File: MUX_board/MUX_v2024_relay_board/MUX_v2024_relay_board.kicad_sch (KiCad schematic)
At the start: 21 parts, among them J1 A B M N, J2 Relays Pwr, J3 I2C, J4 Screw_Terminal_01x08, J5 A B M N, J6 I2C, U1 24LC02, U2 MCP23017_SP, U3 MCP23017_SP, U4 MCP23017_SP, U5 4052, U6 4052, U7 4052, U8 4052

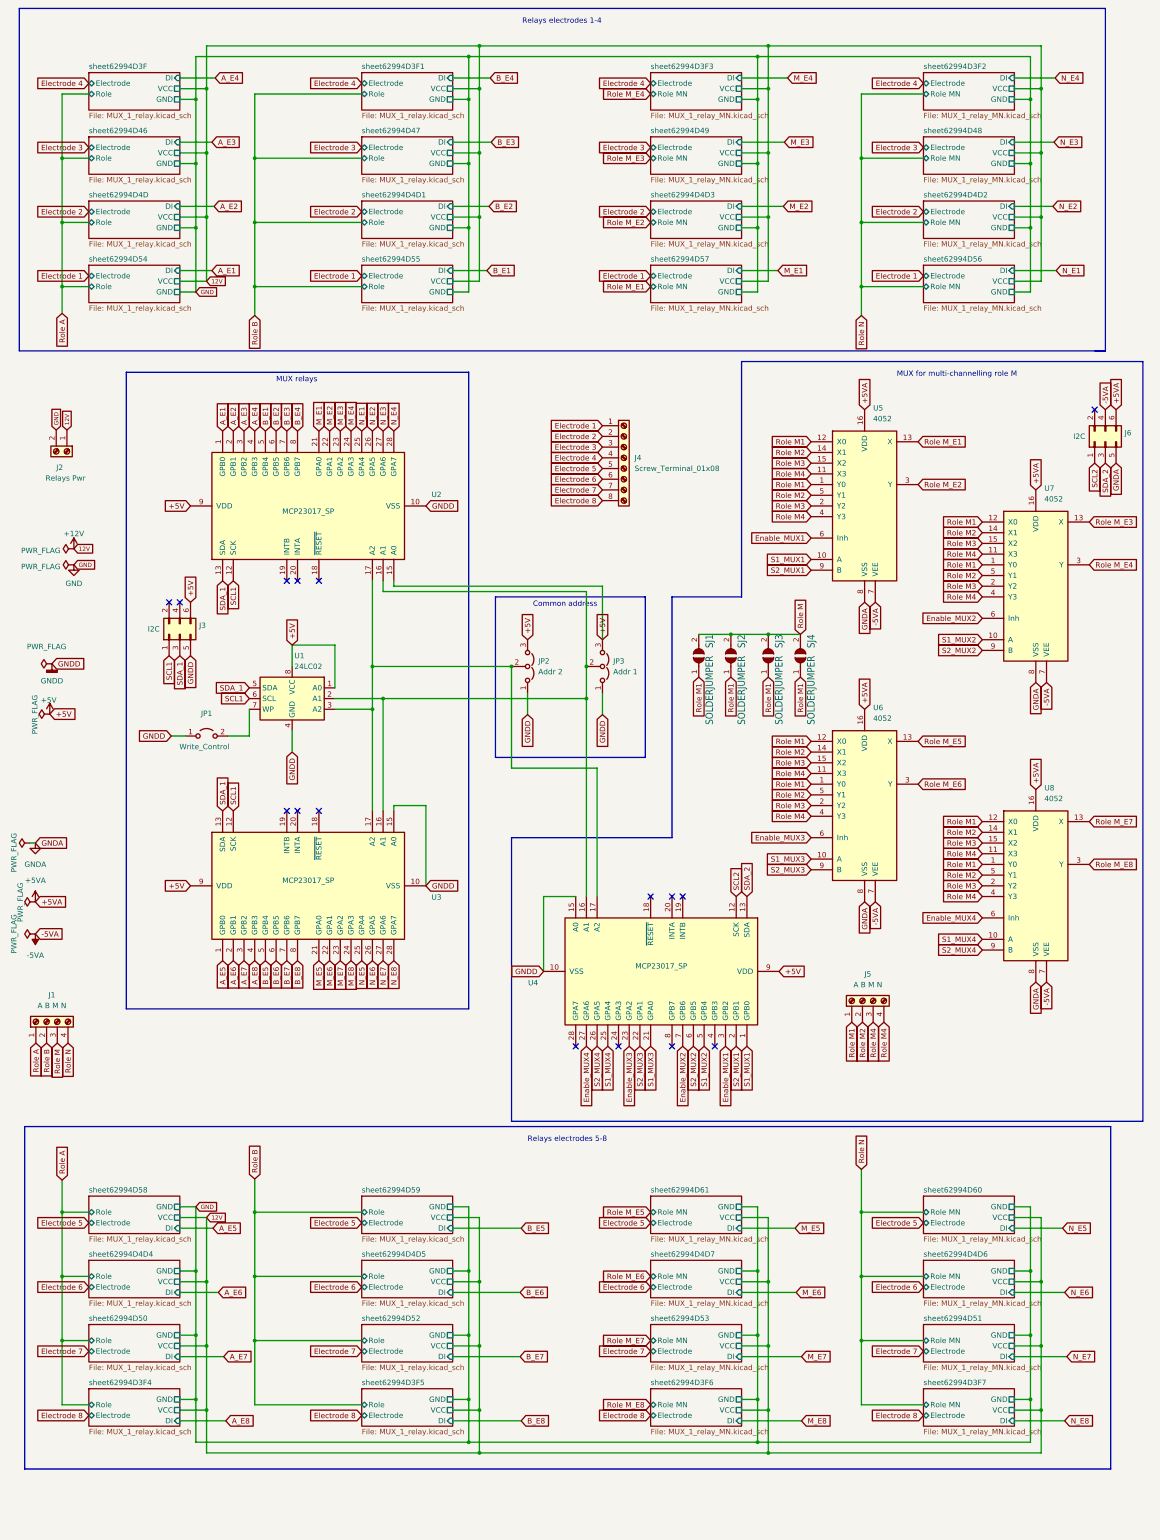
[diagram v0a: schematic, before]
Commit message: Modifies schematics for scenario with single MN relays and analog multiplexers for roles M1 M2 and N. This assumes that the measurement board is modified to allow simultaneous measurements of M1 and M2 on the ADS, while N is put on the GND. The multiplexers would allow to cycle between a series of M1 and M2. See issue #60.
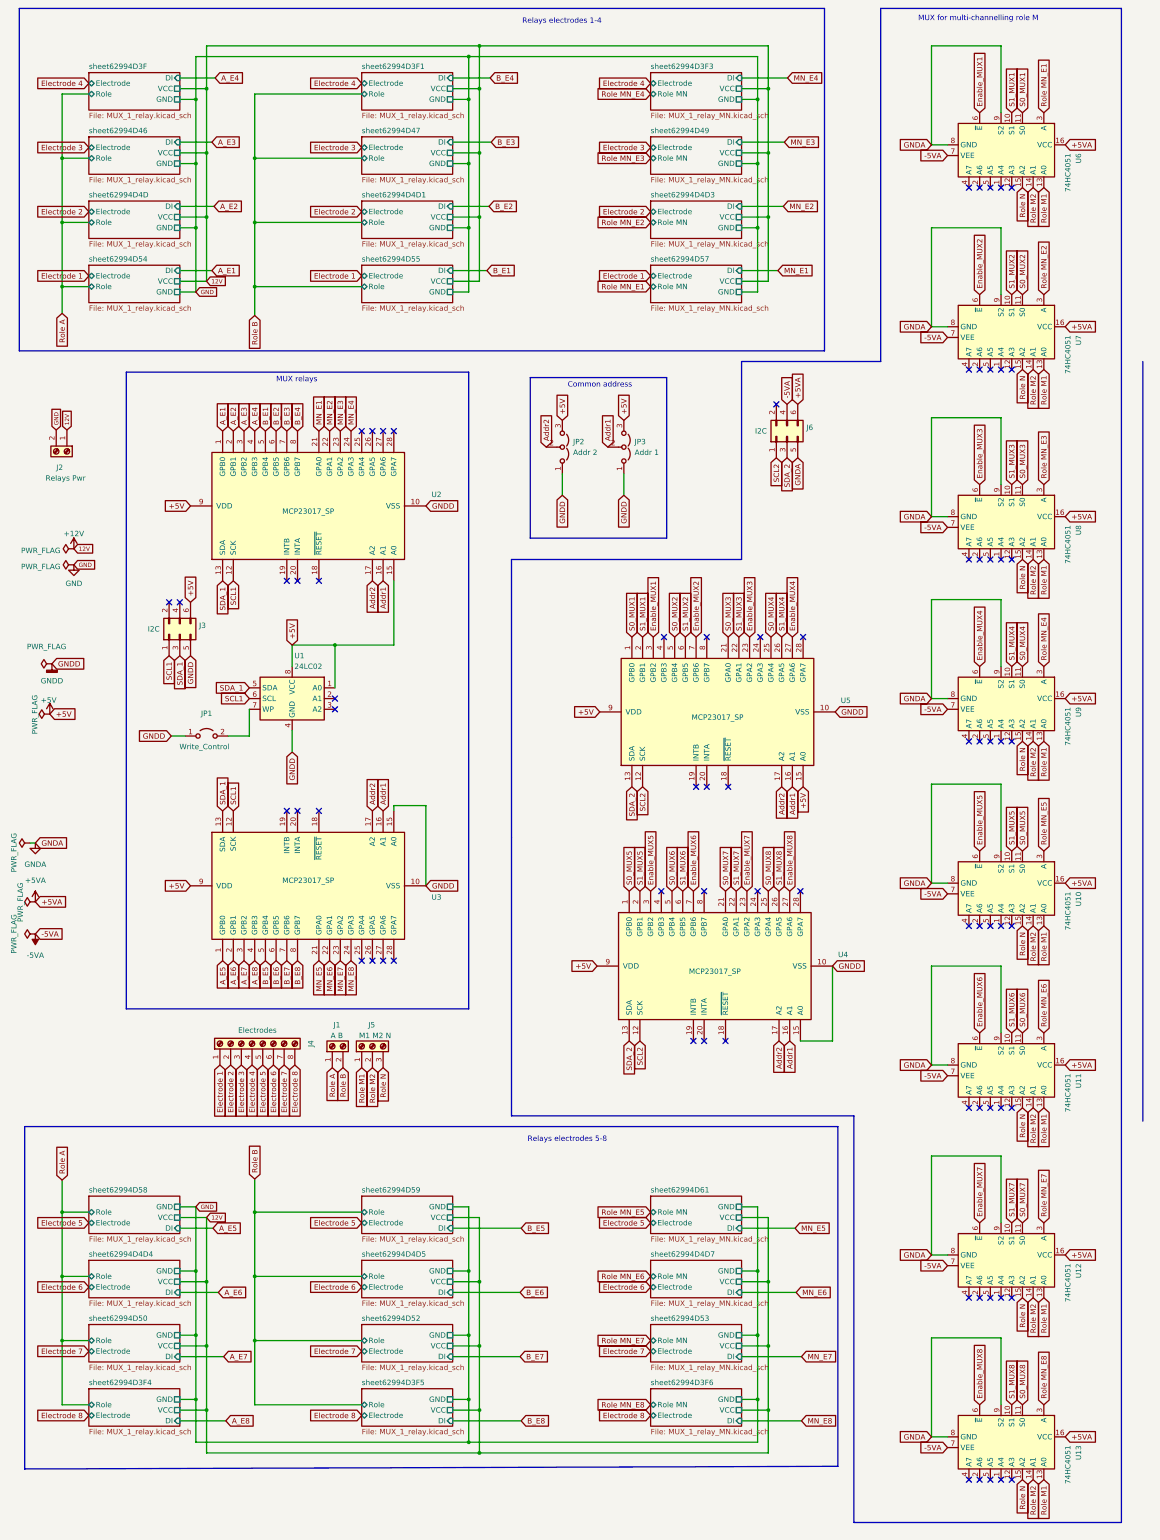
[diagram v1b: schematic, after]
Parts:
- removed J1, J5: A B M N, TerminalBlock_Phoenix:TerminalBlock_Phoenix_MKDS-1,5-4_1x04_P5.00mm_Horizontal, symbol Connector:Screw_Terminal_01x04
- removed SJ1, SJ2, SJ3, SJ4: SOLDERJUMPER, Adafruit TCA9548A:SOLDERJUMPER_ARROW_NOPASTE, symbol Adafruit TCA9548A-eagle-import:SOLDERJUMPER
- removed U5, U6, U7, U8: 4052, Package_DIP:DIP-16_W7.62mm, symbol 4xxx:4052
- added J1: A B, symbol Connector:Screw_Terminal_01x02
- added J5: M1 M2 N, symbol Connector:Screw_Terminal_01x03
- added U10, U11, U12, U13, U6, U7, U8, U9: 74HC4051, symbol 74xx:74HC4051
- added U5: MCP23017_SP, Package_DIP:DIP-28_W7.62mm, symbol Interface_Expansion:MCP23017_SP
- J4: value Screw_Terminal_01x08 -> Electrodes
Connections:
- net +5V: now also U5.15 (A0), U5.9 (VDD)
- net +5VA: now also U10.16 (VCC), U11.16 (VCC), U12.16 (VCC), U13.16 (VCC), U6.16 (VCC), U7.16 (VCC), U8.16 (VCC), U9.16 (VCC)
- net -5VA: now also U10.7 (VEE), U11.7 (VEE), U12.7 (VEE), U13.7 (VEE), U6.7 (VEE), U7.7 (VEE), U8.7 (VEE), U9.7 (VEE)
- net Enable_MUX1: now also U5.3 (GPB2), U6.6 (~{E}); no longer U4.3 (GPB2)
- net Enable_MUX2: now also U5.7 (GPB6), U7.6 (~{E}); no longer U4.7 (GPB6)
- net Enable_MUX3: now also U5.23 (GPA2), U8.6 (~{E}); no longer U4.23 (GPA2)
- net Enable_MUX4: now also U5.27 (GPA6), U9.6 (~{E}); no longer U4.27 (GPA6)
- net GNDA: now also U10.8 (GND), U10.9 (S2), U11.8 (GND), U11.9 (S2), U12.8 (GND), U12.9 (S2), U13.8 (GND), U13.9 (S2), U6.8 (GND), U6.9 (S2), U7.8 (GND), U7.9 (S2), U8.8 (GND), U8.9 (S2), U9.8 (GND), U9.9 (S2)
- net GNDD: now also U5.10 (VSS)
- net Role A: now also J1.1 (Pin_1)
- net Role B: now also J1.2 (Pin_2)
- net Role M1: now also J5.1 (Pin_1), U10.13 (A0), U11.13 (A0), U12.13 (A0), U13.13 (A0), U6.13 (A0), U7.13 (A0), U8.13 (A0), U9.13 (A0)
- net Role M2: now also J5.2 (Pin_2), U10.14 (A1), U11.14 (A1), U12.14 (A1), U13.14 (A1), U6.14 (A1), U7.14 (A1), U8.14 (A1), U9.14 (A1)
- net Role N: now also J5.3 (Pin_3), U10.15 (A2), U11.15 (A2), U12.15 (A2), U13.15 (A2), U6.15 (A2), U7.15 (A2), U8.15 (A2), U9.15 (A2)
- net S1_MUX1: now also U5.2 (GPB1), U6.10 (S1); no longer U4.1 (GPB0)
- net S1_MUX2: now also U5.6 (GPB5), U7.10 (S1); no longer U4.5 (GPB4)
- net S1_MUX3: now also U5.22 (GPA1), U8.10 (S1); no longer U4.21 (GPA0)
- net S1_MUX4: now also U5.26 (GPA5), U9.10 (S1); no longer U4.25 (GPA4)
- net SCL2: now also U5.12 (SCK)
- net SDA_2: now also U5.13 (SDA)
- net Addr2: now reaches JP2.2 (C), U2.17 (A2), U3.17 (A2), U4.17 (A2)
- net Addr2: now also U5.17 (A2); no longer U1.3 (A2)
- net Addr1: now reaches JP3.2 (C), U2.16 (A1), U3.16 (A1), U4.16 (A1)
- net Addr1: now also U5.16 (A1); no longer U1.2 (A1)
- net M_E1 renamed MN_E1
- net M_E2 renamed MN_E2
- net M_E3 renamed MN_E3
- net M_E4 renamed MN_E4
- net M_E5 renamed MN_E5
- net M_E6 renamed MN_E6
- net M_E7 renamed MN_E7
- net M_E8 renamed MN_E8
- net N_E1: no longer names the net of U2.25 (GPA4)
- net N_E2: no longer names the net of U2.26 (GPA5)
- net N_E3: no longer names the net of U2.27 (GPA6)
- net N_E4: no longer names the net of U2.28 (GPA7)
- net N_E5: no longer names the net of U3.25 (GPA4)
- net N_E6: no longer names the net of U3.26 (GPA5)
- net N_E7: no longer names the net of U3.27 (GPA6)
- net N_E8: no longer names the net of U3.28 (GPA7)
- net S2_MUX1 renamed S1_MUX5
- net S1_MUX5: now also U10.10 (S1)
- net S2_MUX2 renamed S1_MUX6
- net S1_MUX6: now also U11.10 (S1)
- net S2_MUX3 renamed S1_MUX7
- net S1_MUX7: now also U12.10 (S1)
- net S2_MUX4 renamed S1_MUX8
- net S1_MUX8: now also U13.10 (S1)
- new net Enable_MUX5: U10.6 (~{E}), U4.3 (GPB2)
- new net Enable_MUX6: U11.6 (~{E}), U4.7 (GPB6)
- new net Enable_MUX7: U12.6 (~{E}), U4.23 (GPA2)
- new net Enable_MUX8: U13.6 (~{E}), U4.27 (GPA6)
- new net Role MN_E1: U6.3 (A)
- new net Role MN_E2: U7.3 (A)
- new net Role MN_E3: U8.3 (A)
- new net Role MN_E4: U9.3 (A)
- new net Role MN_E5: U10.3 (A)
- new net Role MN_E6: U11.3 (A)
- new net Role MN_E7: U12.3 (A)
- new net Role MN_E8: U13.3 (A)
- new net S0_MUX1: U5.1 (GPB0), U6.11 (S0)
- new net S0_MUX2: U5.5 (GPB4), U7.11 (S0)
- new net S0_MUX3: U5.21 (GPA0), U8.11 (S0)
- new net S0_MUX4: U5.25 (GPA4), U9.11 (S0)
- new net S0_MUX5: U10.11 (S0), U4.1 (GPB0)
- new net S0_MUX6: U11.11 (S0), U4.5 (GPB4)
- new net S0_MUX7: U12.11 (S0), U4.21 (GPA0)
- new net S0_MUX8: U13.11 (S0), U4.25 (GPA4)
- no-connect marks 16 -> 73
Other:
- removed sheet sheet62994D3F2
- removed sheet sheet62994D3F7
- removed sheet sheet62994D48
- removed sheet sheet62994D4D2
- removed sheet sheet62994D4D6
- removed sheet sheet62994D51
- removed sheet sheet62994D56
- removed sheet sheet62994D60
- moved on the sheet: J4, J6, JP2, JP3, U4
